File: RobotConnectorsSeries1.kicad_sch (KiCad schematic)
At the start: 8 parts

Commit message: Add latest findings
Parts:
- S1-J13, S1-J14, S1-J15, S1-J17, S1-J7: now not fitted; now left out of the parts list
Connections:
- net MC_HALL_SENSOR.U: now also S1-J13.7 (Pin_7); no longer S1-J13.4 (Pin_4)
- net MC_HALL_SENSOR.W: now also S1-J13.4 (Pin_4); no longer S1-J13.7 (Pin_7)
- net MC_PHASE.U: now also S1-J13.5 (Pin_5); no longer S1-J13.1 (Pin_1)
- net MC_PHASE.W: now also S1-J13.1 (Pin_1); no longer S1-J13.5 (Pin_5)
- net BMS_SPI_CLK renamed BMS_I2C_SDA
- net BMS_SPI_MISO renamed BMS_I2C_SCL
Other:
- note added: "YES, twisted colors!"
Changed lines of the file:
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@@
 		(comment 1 "This design is licensed under CC BY-NC 4.0")
 	)
+	(text "YES, twisted colors!"
+		(exclude_from_sim no)
+		(at 95.504 32.258 0)
+		(effects
+			(font
+				(size 1.27 1.27)
+				(thickness 0.254)
+				(bold yes)
+				(color 255 0 0 1)
+			)
+		)
+	)
 	(text "H2"
 		(exclude_from_sim no)
@@
 	(wire
 		(pts
-			(xy 102.87 87.63) (xy 62.23 87.63)
+			(xy 62.23 87.63) (xy 102.87 87.63)
 		)
 		(stroke
@@
 	)
 	(label "MC_PHASE.W"
-		(at 44.45 74.93 0)
+		(at 44.45 77.47 0)
 		(effects
 			(font
@@
 	)
 	(label "MC_HALL_SENSOR.W"
-		(at 102.87 82.55 180)
+		(at 101.6 87.63 180)
 		(effects
 			(font
@@
 	)
 	(label "MC_HALL_SENSOR.V"
-		(at 102.87 85.09 180)
+		(at 101.6 85.09 180)
 		(effects
 			(font
@@
 	)
 	(label "MC_PHASE.U"
-		(at 44.45 77.47 0)
+		(at 44.45 74.93 0)
 		(effects
 			(font
@@
 	)
 	(label "MC_HALL_SENSOR.U"
-		(at 102.87 87.63 180)
+		(at 101.6 82.55 180)
 		(effects
 			(font
@@
 		)
 	)
-	(hierarchical_label "BMS_SPI_CLK"
+	(hierarchical_label "BMS_I2C_SCL"
 		(shape input)
-		(at 86.36 35.56 0)
+		(at 86.36 38.1 0)
 		(effects
 			(font
@@
 			(justify left)
 		)
-		(property "CableColor" "Yellow"
-			(at 77.47 34.544 0)
+		(property "CableColor" "Green"
+			(at 78.232 37.084 0)
 			(effects
 				(font
@@
 		)
 	)
-	(hierarchical_label "BMS_SPI_MISO"
+	(hierarchical_label "BMS_I2C_SDA"
 		(shape output)
-		(at 86.36 38.1 0)
+		(at 86.36 35.56 0)
 		(effects
 			(font
@@
 			(justify left)
 		)
-		(property "CableColor" "Green"
-			(at 77.978 37.084 0)
+		(property "CableColor" "Yellow"
+			(at 77.978 34.544 0)
 			(effects
 				(font
@@
 		(unit 1)
 		(exclude_from_sim no)
-		(in_bom yes)
+		(in_bom no)
 		(on_board yes)
-		(dnp no)
+		(dnp yes)
 		(property "Reference" "S1-J15"
 			(at 70.866 131.572 0)
@@
 		(unit 1)
 		(exclude_from_sim no)
-		(in_bom yes)
+		(in_bom no)
 		(on_board yes)
-		(dnp no)
+		(dnp yes)
 		(property "Reference" "S1-J13"
 			(at 71.374 65.786 0)
@@
 		(unit 1)
 		(exclude_from_sim no)
-		(in_bom yes)
+		(in_bom no)
 		(on_board yes)
-		(dnp no)
+		(dnp yes)
 		(property "Reference" "S1-J7"
 			(at 245.364 20.828 0)
@@
 		(unit 1)
 		(exclude_from_sim no)
-		(in_bom yes)
+		(in_bom no)
 		(on_board yes)
-		(dnp no)
+		(dnp yes)
 		(property "Reference" "S1-J14"
 			(at 70.866 100.838 0)
@@
 		(unit 1)
 		(exclude_from_sim no)
-		(in_bom yes)
+		(in_bom no)
 		(on_board yes)
-		(dnp no)
+		(dnp yes)
 		(property "Reference" "S1-J17"
 			(at 71.12 29.21 0)

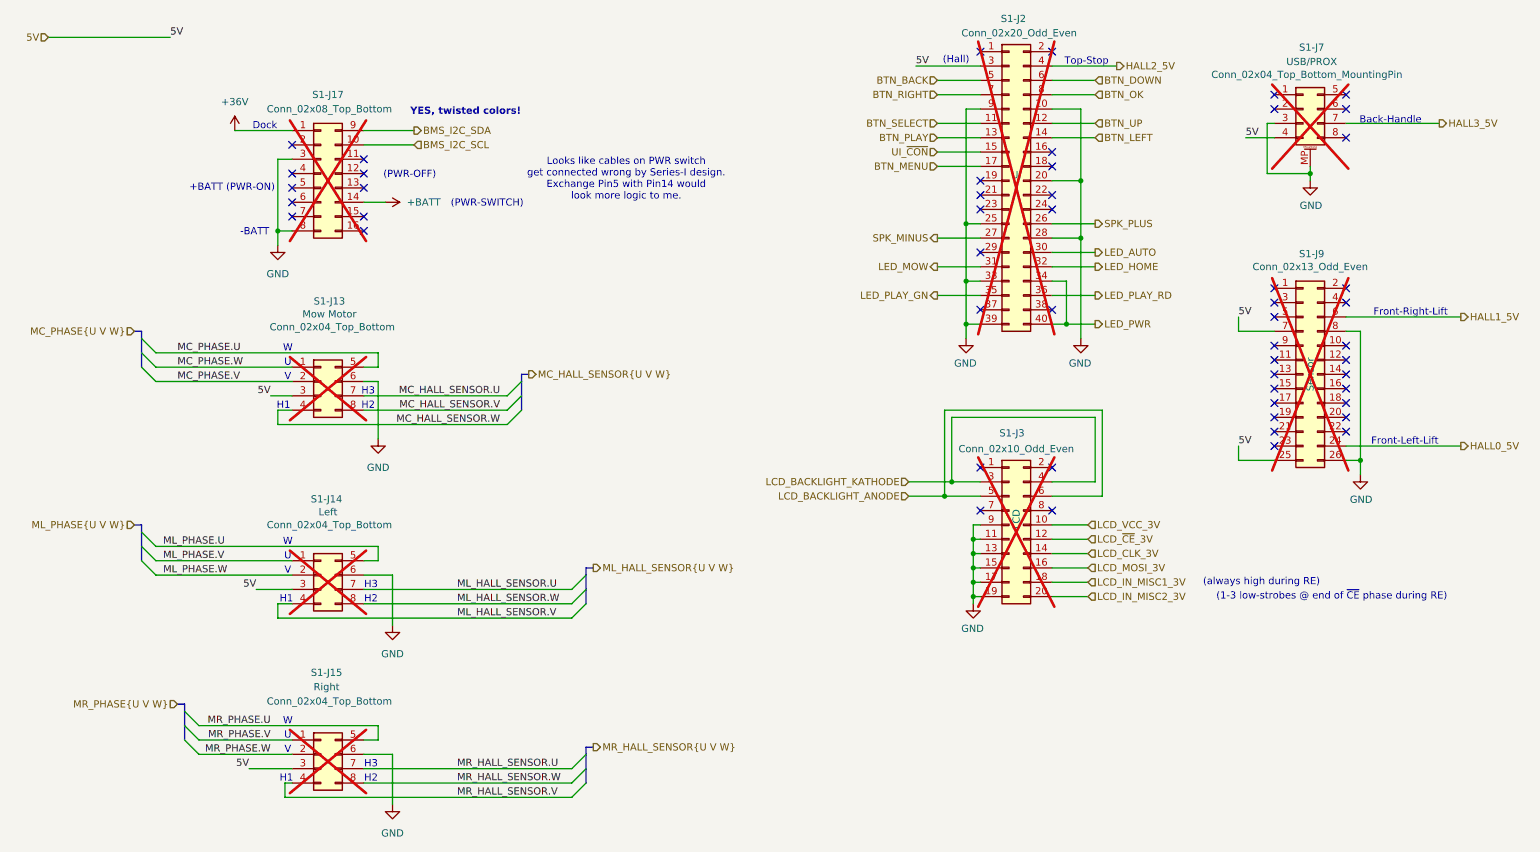
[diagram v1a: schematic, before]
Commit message: Prepare for next production - Slightly adapt part selection - Add TC2050 holes
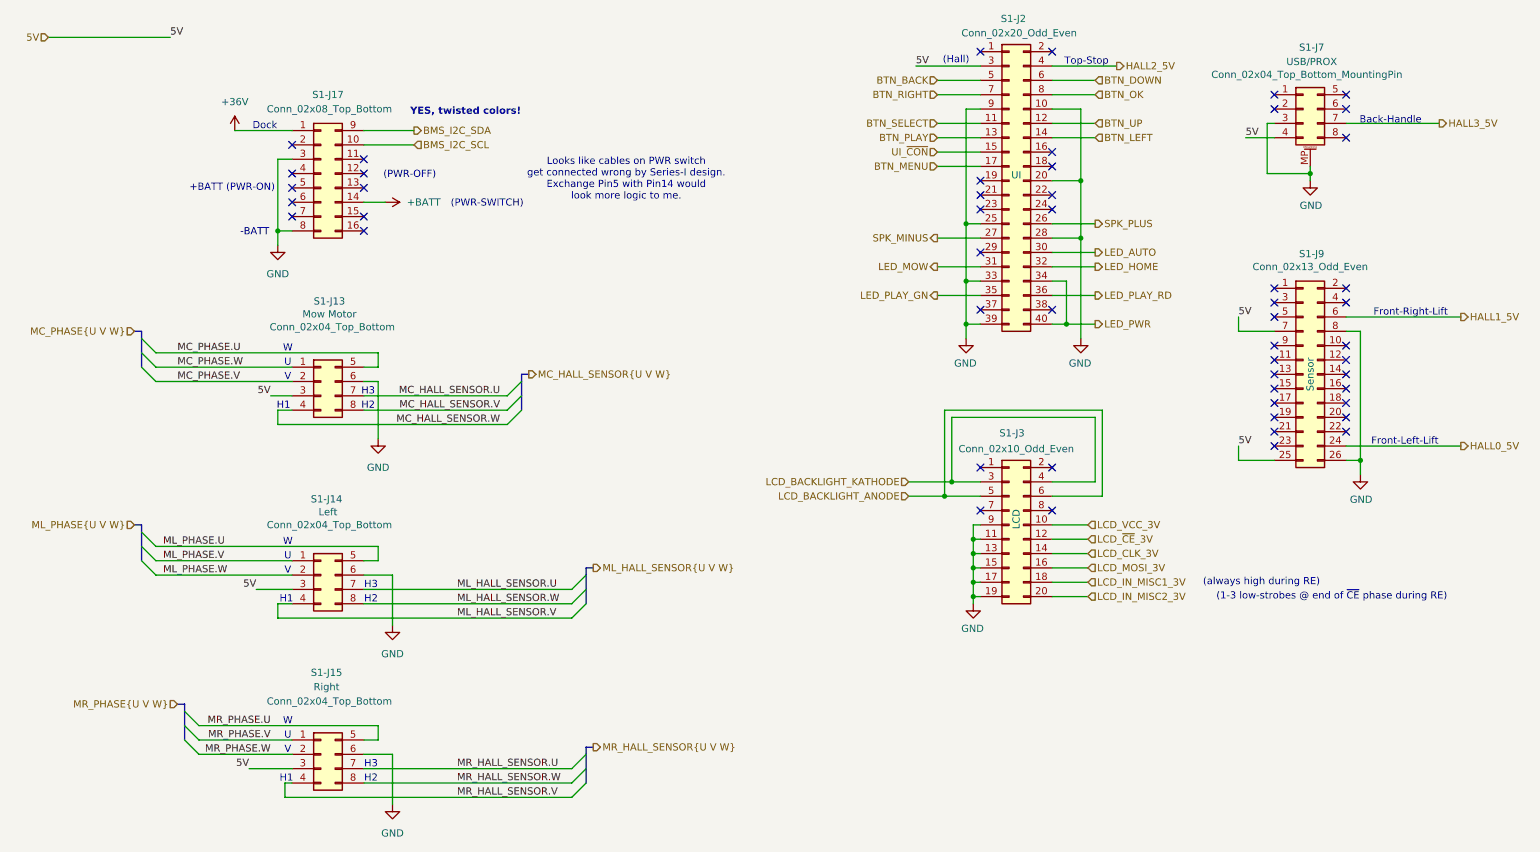
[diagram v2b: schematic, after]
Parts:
- S1-J13, S1-J14, S1-J15: JLC C293503 -> (none); LCSC Part # (none) -> C293503; now fitted; now in the parts list
- S1-J17: JLC C5339222 -> (none); LCSC Part # (none) -> C5339222; now fitted; now in the parts list
- S1-J2: JLC C3330369 -> (none); LCSC Part # (none) -> C5166238; MFPN (none) -> 5-104068-4; now fitted; now in the parts list
- S1-J3: LCSC Part # (none) -> C306145; now fitted; now in the parts list
- S1-J7: MF (none) -> Molex; Manufacturer Molex -> (none); now fitted; now in the parts list
- S1-J9: MF (none) -> Megastar; Manufacturer Megastar -> (none); now fitted; now in the parts list
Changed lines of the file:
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@@
 		(unit 1)
 		(exclude_from_sim no)
-		(in_bom no)
+		(in_bom yes)
 		(on_board yes)
-		(dnp yes)
+		(dnp no)
 		(property "Reference" "S1-J15"
 			(at 70.866 131.572 0)
@@
 			)
 		)
-		(property "JLC" "C293503"
-			(at 69.85 146.05 0)
-			(effects
-				(font
-					(size 1.27 1.27)
-				)
-				(hide yes)
-			)
-		)
-		(property "MPN" ""
-			(at 69.85 146.05 0)
-			(effects
-				(font
-					(size 1.27 1.27)
-				)
-			)
-		)
 		(property "Alternative" ""
 			(at 69.85 146.05 0)
@@
 			)
 		)
-		(property "LCSC" ""
+		(property "LCSC Part #" "C293503"
 			(at 69.85 146.05 0)
 			(effects
@@
 		(unit 1)
 		(exclude_from_sim no)
-		(in_bom no)
+		(in_bom yes)
 		(on_board yes)
-		(dnp yes)
+		(dnp no)
 		(property "Reference" "S1-J13"
 			(at 71.374 65.786 0)
@@
 			)
 		)
-		(property "JLC" "C293503"
-			(at 69.85 80.01 0)
-			(effects
-				(font
-					(size 1.27 1.27)
-				)
-				(hide yes)
-			)
-		)
-		(property "MPN" ""
-			(at 69.85 80.01 0)
-			(effects
-				(font
-					(size 1.27 1.27)
-				)
-			)
-		)
 		(property "Alternative" ""
 			(at 69.85 80.01 0)
@@
 			)
 		)
-		(property "LCSC" ""
+		(property "LCSC Part #" "C293503"
 			(at 69.85 80.01 0)
 			(effects
@@
 		(unit 1)
 		(exclude_from_sim no)
-		(in_bom no)
+		(in_bom yes)
 		(on_board yes)
-		(dnp yes)
+		(dnp no)
 		(property "Reference" "S1-J9"
 			(at 245.364 57.404 0)
@@
 			)
 		)
-		(property "Manufacturer" "Megastar"
-			(at 243.84 78.74 0)
-			(effects
-				(font
-					(size 1.27 1.27)
-				)
-				(hide yes)
-			)
-		)
 		(property "LCSC Part #" "C7501247"
 			(at 243.84 78.74 0)
@@
 			)
 		)
-		(property "LCSC" ""
+		(property "MF" "Megastar"
 			(at 243.84 78.74 0)
 			(effects
@@
 		(unit 1)
 		(exclude_from_sim no)
-		(in_bom no)
+		(in_bom yes)
 		(on_board yes)
-		(dnp yes)
+		(dnp no)
 		(property "Reference" "S1-J3"
 			(at 192.278 89.154 0)
@@
 			)
 		)
-		(property "MPN" ""
-			(at 191.77 105.41 0)
-			(effects
-				(font
-					(size 1.27 1.27)
-				)
-			)
-		)
 		(property "Alternative" ""
 			(at 191.77 105.41 0)
@@
 			)
 		)
-		(property "LCSC" ""
+		(property "LCSC Part #" "C306145"
 			(at 191.77 105.41 0)
 			(effects
@@
 		(unit 1)
 		(exclude_from_sim no)
-		(in_bom no)
+		(in_bom yes)
 		(on_board yes)
-		(dnp yes)
+		(dnp no)
 		(property "Reference" "S1-J7"
 			(at 245.364 20.828 0)
@@
 			)
 		)
-		(property "Manufacturer" "Molex"
-			(at 243.84 31.75 0)
-			(effects
-				(font
-					(size 1.27 1.27)
-				)
-				(hide yes)
-			)
-		)
 		(property "MFPN" "430450818"
 			(at 243.84 31.75 0)
@@
 			)
 		)
-		(property "LCSC" ""
+		(property "MF" "Molex"
 			(at 243.84 31.75 0)
 			(effects
@@
 		(unit 1)
 		(exclude_from_sim no)
-		(in_bom no)
+		(in_bom yes)
 		(on_board yes)
-		(dnp yes)
+		(dnp no)
 		(property "Reference" "S1-J2"
 			(at 192.532 15.748 0)
@@
 			)
 		)
-		(property "Description" "TE Connectivity, AMPMODU System 50, 5-104068-4"
+		(property "Description" "Generic connector, double row, 02x20, odd/even pin numbering scheme (row 1 odd numbers, row 2 even numbers), script generated (kicad-library-utils/schlib/autogen/connector/)"
 			(at 191.77 44.45 0)
 			(effects
@@
 			)
 		)
-		(property "JLC" "C3330369"
+		(property "MFPN" "5-104068-4"
 			(at 191.77 44.45 0)
 			(effects
@@
 				)
 				(hide yes)
-			)
-		)
-		(property "MPN" ""
-			(at 191.77 44.45 0)
-			(effects
-				(font
-					(size 1.27 1.27)
-				)
 			)
 		)
@@
 			)
 		)
-		(property "LCSC" ""
+		(property "LCSC Part #" "C5166238"
 			(at 191.77 44.45 0)
 			(effects
@@
 		(unit 1)
 		(exclude_from_sim no)
-		(in_bom no)
+		(in_bom yes)
 		(on_board yes)
-		(dnp yes)
+		(dnp no)
 		(property "Reference" "S1-J14"
 			(at 70.866 100.838 0)
@@
 			)
 		)
-		(property "JLC" "C293503"
-			(at 69.85 114.3 0)
-			(effects
-				(font
-					(size 1.27 1.27)
-				)
-				(hide yes)
-			)
-		)
-		(property "MPN" ""
-			(at 69.85 114.3 0)
-			(effects
-				(font
-					(size 1.27 1.27)
-				)
-			)
-		)
 		(property "Alternative" ""
 			(at 69.85 114.3 0)
@@
 			)
 		)
-		(property "LCSC" ""
+		(property "LCSC Part #" "C293503"
 			(at 69.85 114.3 0)
 			(effects
@@
 		(unit 1)
 		(exclude_from_sim no)
-		(in_bom no)
+		(in_bom yes)
 		(on_board yes)
-		(dnp yes)
+		(dnp no)
 		(property "Reference" "S1-J17"
 			(at 71.12 29.21 0)
@@
 			)
 		)
-		(property "JLC" "C5339222"
-			(at 69.85 43.18 0)
-			(effects
-				(font
-					(size 1.27 1.27)
-				)
-				(hide yes)
-			)
-		)
 		(property "Alternative" ""
 			(at 69.85 43.18 0)
@@
 			)
 		)
-		(property "LCSC" ""
+		(property "LCSC Part #" "C5339222"
 			(at 69.85 43.18 0)
 			(effects

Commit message: Production state
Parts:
- S1-J2, S1-J3: now not fitted; now left out of the parts list
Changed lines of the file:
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@@
 	(title_block
 		(title "OpenMower SABO Carrierboard for Series I & II")
-		(date "2025-10-12")
+		(date "2026-04-04")
 		(rev "v0.4")
 		(company "Apeheanger <joerg@ebeling.ws> for OpenMower")
@@
 		(unit 1)
 		(exclude_from_sim no)
-		(in_bom yes)
+		(in_bom no)
 		(on_board yes)
-		(dnp no)
+		(dnp yes)
 		(property "Reference" "S1-J3"
 			(at 192.278 89.154 0)
@@
 		(unit 1)
 		(exclude_from_sim no)
-		(in_bom yes)
+		(in_bom no)
 		(on_board yes)
-		(dnp no)
+		(dnp yes)
 		(property "Reference" "S1-J2"
 			(at 192.532 15.748 0)

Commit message: KiCAD 10.x, Mow-ESC-Fuse, Improve power traces
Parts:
- S1-J3: DigiKey A33555-ND -> (none); Digikey (none) -> A33555-ND
